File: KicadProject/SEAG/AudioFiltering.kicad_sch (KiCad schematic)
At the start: 8 parts, among them U2 ${SIM.PARAMS}

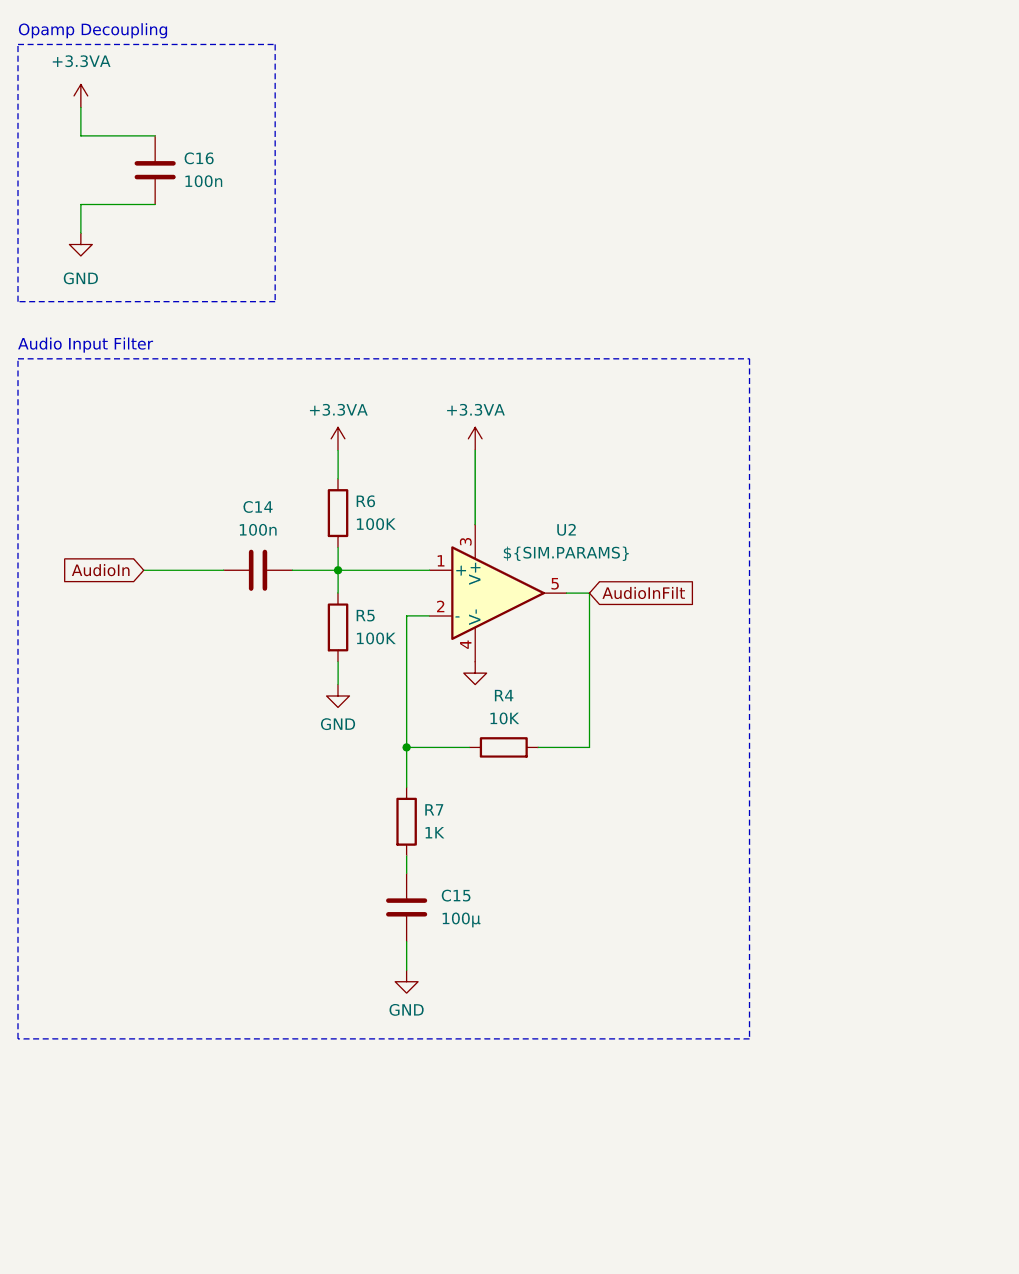
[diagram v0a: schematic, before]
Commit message: Added ESD protection, extra filtering with ferrite bead
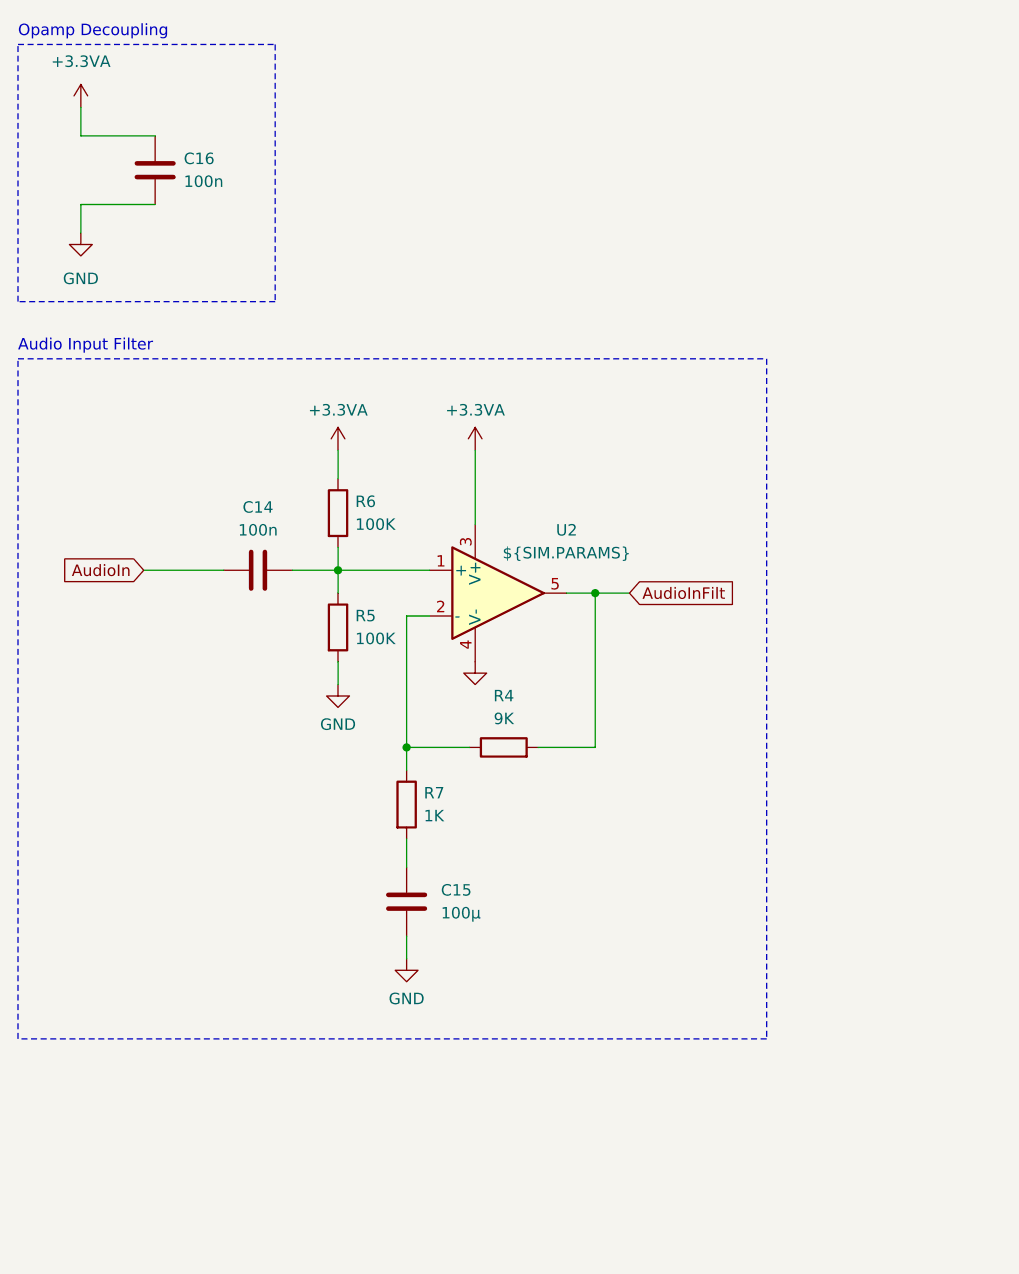
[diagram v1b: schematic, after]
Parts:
- R4: value 10K -> 9K
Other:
- moved on the sheet: C15, R7
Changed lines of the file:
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@@
 (kicad_sch (version 20230121) (generator eeschema)
   (paper "A4")
+  (junction (at 81.28 81.915) (diameter 0) (color 0 0 0 0)
+  )
   (junction (at 60.325 99.06) (diameter 0) (color 0 0 0 0)
   )
   (junction (at 52.705 79.375) (diameter 0) (color 0 0 0 0)
   )
-  (wire (pts (xy 74.93 99.06) (xy 80.645 99.06))
-    (stroke (width 0) (type default))
-  )
-  (wire (pts (xy 80.645 81.915) (xy 78.105 81.915))
+  (wire (pts (xy 74.93 99.06) (xy 81.28 99.06))
     (stroke (width 0) (type default))
   )
@@
     (stroke (width 0) (type default))
   )
-  (wire (pts (xy 60.325 99.06) (xy 60.325 103.505))
+  (wire (pts (xy 60.325 99.06) (xy 60.325 101.6))
+    (stroke (width 0) (type default))
+  )
+  (wire (pts (xy 81.28 81.915) (xy 85.09 81.915))
     (stroke (width 0) (type default))
   )
@@
     (stroke (width 0) (type default))
   )
-  (wire (pts (xy 60.325 111.125) (xy 60.325 113.03))
+  (wire (pts (xy 60.325 109.22) (xy 60.325 112.395))
     (stroke (width 0) (type default))
   )
@@
     (stroke (width 0) (type default))
   )
-  (wire (pts (xy 80.645 99.06) (xy 80.645 81.915))
-    (stroke (width 0) (type default))
-  )
-  (wire (pts (xy 60.325 120.65) (xy 60.325 123.825))
+  (wire (pts (xy 78.105 81.915) (xy 81.28 81.915))
+    (stroke (width 0) (type default))
+  )
+  (wire (pts (xy 60.325 120.015) (xy 60.325 122.555))
     (stroke (width 0) (type default))
   )
@@
     (stroke (width 0) (type default))
   )
-  (rectangle (start 17.145 55.88) (end 98.425 131.445)
+  (wire (pts (xy 81.28 81.915) (xy 81.28 99.06))
+    (stroke (width 0) (type default))
+  )
+  (rectangle (start 17.145 55.88) (end 100.33 131.445)
     (stroke (width 0) (type dash))
     (fill (type none))
@@
     )
   )
-  (global_label "AudioInFilt" (shape input) (at 80.645 81.915 0) (fields_autoplaced)
+  (global_label "AudioInFilt" (shape input) (at 85.09 81.915 0) (fields_autoplaced)
     (effects (font (size 1.27 1.27)) (justify left))
-    (property "Intersheetrefs" "${INTERSHEET_REFS}" (at 93.6087 81.915 0)
+    (property "Intersheetrefs" "${INTERSHEET_REFS}" (at 98.0537 81.915 0)
       (effects (font (size 1.27 1.27)) (justify left) hide)
     )
@@
     )
   )
-  (symbol (lib_id "Device:R") (at 60.325 107.315 0) (unit 1)
-    (in_bom yes) (on_board yes) (dnp no) (fields_autoplaced)
-    (property "Reference" "R7" (at 62.23 106.045 0)
-      (effects (font (size 1.27 1.27)) (justify left))
-    )
-    (property "Value" "1K" (at 62.23 108.585 0)
-      (effects (font (size 1.27 1.27)) (justify left))
-    )
-    (property "Footprint" "Resistor_SMD:R_0805_2012Metric" (at 58.547 107.315 90)
-      (effects (font (size 1.27 1.27)) hide)
-    )
-    (property "Datasheet" "~" (at 60.325 107.315 0)
+  (symbol (lib_id "Device:R") (at 60.325 105.41 0) (unit 1)
+    (in_bom yes) (on_board yes) (dnp no) (fields_autoplaced)
+    (property "Reference" "R7" (at 62.23 104.14 0)
+      (effects (font (size 1.27 1.27)) (justify left))
+    )
+    (property "Value" "1K" (at 62.23 106.68 0)
+      (effects (font (size 1.27 1.27)) (justify left))
+    )
+    (property "Footprint" "Resistor_SMD:R_0805_2012Metric" (at 58.547 105.41 90)
+      (effects (font (size 1.27 1.27)) hide)
+    )
+    (property "Datasheet" "~" (at 60.325 105.41 0)
       (effects (font (size 1.27 1.27)) hide)
     )
@@
     )
   )
-  (symbol (lib_id "power:GND") (at 60.325 123.825 0) (unit 1)
-    (in_bom yes) (on_board yes) (dnp no) (fields_autoplaced)
-    (property "Reference" "#PWR022" (at 60.325 130.175 0)
-      (effects (font (size 1.27 1.27)) hide)
-    )
-    (property "Value" "GND" (at 60.325 128.27 0)
-      (effects (font (size 1.27 1.27)))
-    )
-    (property "Footprint" "" (at 60.325 123.825 0)
-      (effects (font (size 1.27 1.27)) hide)
-    )
-    (property "Datasheet" "" (at 60.325 123.825 0)
+  (symbol (lib_id "power:GND") (at 60.325 122.555 0) (unit 1)
+    (in_bom yes) (on_board yes) (dnp no) (fields_autoplaced)
+    (property "Reference" "#PWR022" (at 60.325 128.905 0)
+      (effects (font (size 1.27 1.27)) hide)
+    )
+    (property "Value" "GND" (at 60.325 127 0)
+      (effects (font (size 1.27 1.27)))
+    )
+    (property "Footprint" "" (at 60.325 122.555 0)
+      (effects (font (size 1.27 1.27)) hide)
+    )
+    (property "Datasheet" "" (at 60.325 122.555 0)
       (effects (font (size 1.27 1.27)) hide)
     )
@@
       (effects (font (size 1.27 1.27)))
     )
-    (property "Value" "10K" (at 71.12 95.885 90)
+    (property "Value" "9K" (at 71.12 95.885 90)
       (effects (font (size 1.27 1.27)))
     )
@@
     )
   )
-  (symbol (lib_id "Device:C") (at 60.325 116.84 0) (unit 1)
-    (in_bom yes) (on_board yes) (dnp no) (fields_autoplaced)
-    (property "Reference" "C15" (at 64.135 115.57 0)
-      (effects (font (size 1.27 1.27)) (justify left))
-    )
-    (property "Value" "100µ" (at 64.135 118.11 0)
-      (effects (font (size 1.27 1.27)) (justify left))
-    )
-    (property "Footprint" "Capacitor_SMD:C_0805_2012Metric" (at 61.2902 120.65 0)
-      (effects (font (size 1.27 1.27)) hide)
-    )
-    (property "Datasheet" "~" (at 60.325 116.84 0)
-      (effects (font (size 1.27 1.27)) hide)
-    )
+  (symbol (lib_id "Device:C") (at 60.325 116.205 0) (unit 1)
+    (in_bom yes) (on_board yes) (dnp no) (fields_autoplaced)
+    (property "Reference" "C15" (at 64.135 114.935 0)
+      (effects (font (size 1.27 1.27)) (justify left))
+    )
+    (property "Value" "100µ" (at 64.135 117.475 0)
+      (effects (font (size 1.27 1.27)) (justify left))
+    )
+    (property "Footprint" "Capacitor_SMD:C_0805_2012Metric" (at 61.2902 120.015 0)
+      (effects (font (size 1.27 1.27)) hide)
+    )
+    (property "Datasheet" "~" (at 60.325 116.205 0)
+      (effects (font (size 1.27 1.27)) hide)
+    )

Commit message: Finished PCB, stil uncertain about couple things
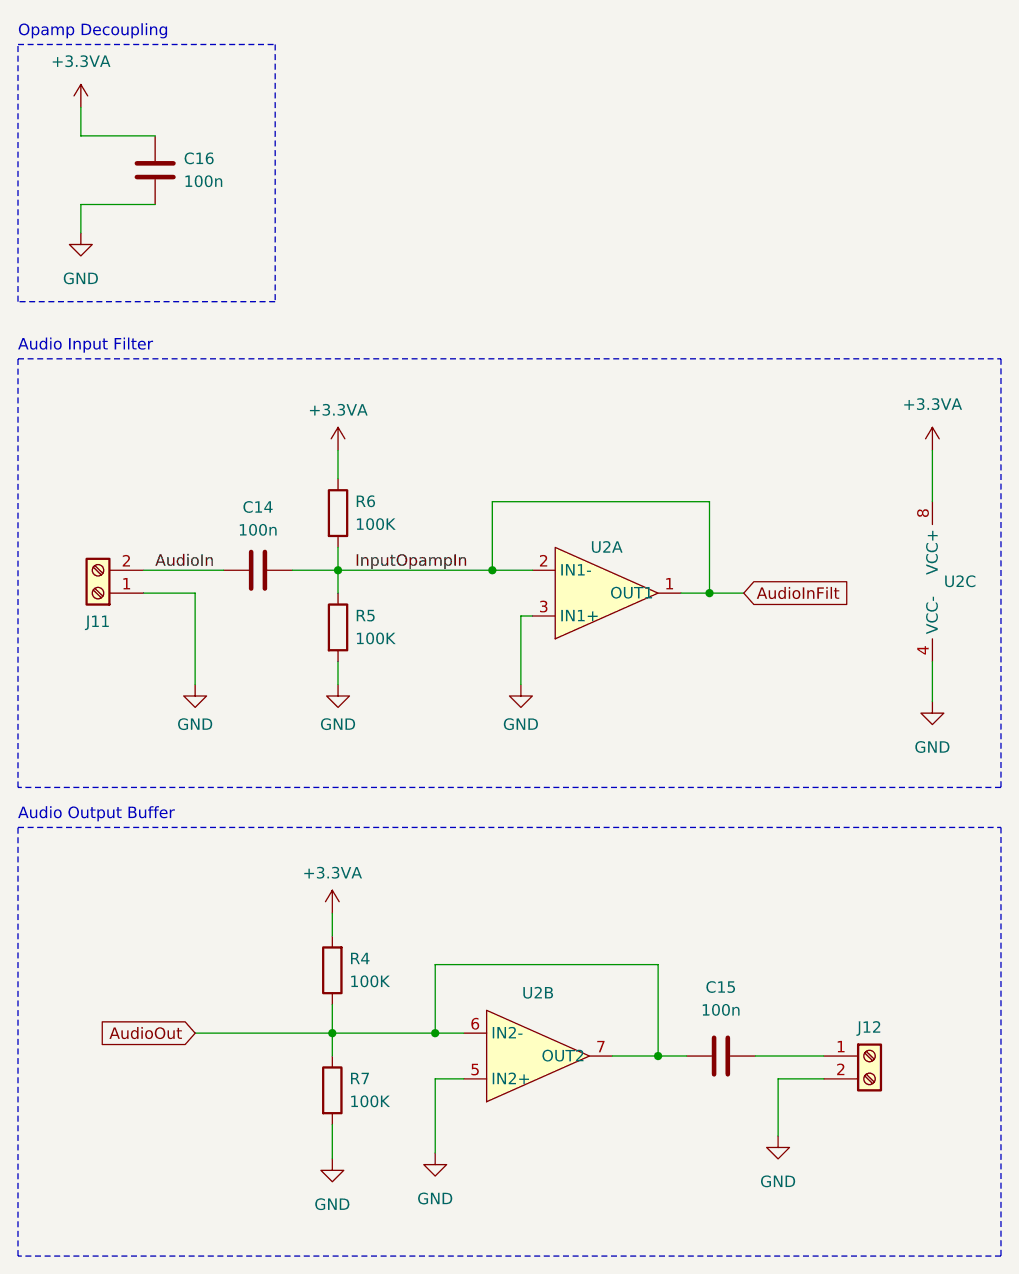
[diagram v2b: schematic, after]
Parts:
- removed U2: ${SIM.PARAMS}, symbol Simulation_SPICE:OPAMP
- added J11, J12: Screw_Terminal_01x02, TerminalBlock_Phoenix:TerminalBlock_Phoenix_MKDS-1,5-2_1x02_P5.00mm_Horizontal, symbol Connector:Screw_Terminal_01x02
- added U2: ~, SamacSys_Parts:SOIC127P600X175-8N, symbol MyLibrary:LM833DGKR_
- C15: value 100µ -> 100n
- R4: value 9K -> 100K
- R7: value 1K -> 100K
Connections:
- net +3.3VA: now also R4.2, U2.8 (VCC+)
- net AudioIn: now also J11.2 (Pin_2)
- net AudioInFilt: now also C14.2, R5.1, R6.2, U2.1 (OUT1), U2.2 (IN1-); no longer R4.2
- net GND: now also R7.2, J11.1 (Pin_1), J12.2 (Pin_2), U2.3 (IN1+), U2.4 (VCC-), U2.5 (IN2+); no longer C15.2
- net AudioOut: now reaches R4.1, R7.1
- net AudioOut: now also C15.1, U2.6 (IN2-), U2.7 (OUT2)
- new net: C15.2, J12.1 (Pin_1)
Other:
- note added: "Audio Output Buffer"

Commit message: PCB rev 2
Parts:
- renumbered C16 to C401, C14 to C402, C15 to C403, R6 to R401, R5 to R402, R4 to R403, R7 to R404
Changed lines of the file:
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@@
   (symbol (lib_id "Device:R") (at 52.07 123.825 180) (unit 1)
     (in_bom yes) (on_board yes) (dnp no) (fields_autoplaced)
-    (property "Reference" "R4" (at 53.975 122.555 0)
+    (property "Reference" "R403" (at 53.975 122.555 0)
       (effects (font (size 1.27 1.27)) (justify right))
     )
@@
       (project "SEAG"
         (path "/37e7da6e-dab5-4e62-b28a-754ec4806405/2395ecb5-6576-49c9-80ea-add07f3bcf94"
-          (reference "R4") (unit 1)
+          (reference "R403") (unit 1)
         )
       )
@@
   (symbol (lib_id "Device:R") (at 52.705 73.025 0) (unit 1)
     (in_bom yes) (on_board yes) (dnp no) (fields_autoplaced)
-    (property "Reference" "R6" (at 54.61 71.755 0)
+    (property "Reference" "R401" (at 54.61 71.755 0)
       (effects (font (size 1.27 1.27)) (justify left))
     )
@@
       (project "SEAG"
         (path "/37e7da6e-dab5-4e62-b28a-754ec4806405/2395ecb5-6576-49c9-80ea-add07f3bcf94"
-          (reference "R6") (unit 1)
+          (reference "R401") (unit 1)
         )
       )
@@
   (symbol (lib_id "Device:C") (at 43.815 79.375 90) (unit 1)
     (in_bom yes) (on_board yes) (dnp no) (fields_autoplaced)
-    (property "Reference" "C14" (at 43.815 72.39 90)
+    (property "Reference" "C402" (at 43.815 72.39 90)
       (effects (font (size 1.27 1.27)))
     )
@@
       (project "SEAG"
         (path "/37e7da6e-dab5-4e62-b28a-754ec4806405/2395ecb5-6576-49c9-80ea-add07f3bcf94"
-          (reference "C14") (unit 1)
+          (reference "C402") (unit 1)
         )
       )
@@
   (symbol (lib_id "Device:R") (at 52.07 137.16 0) (unit 1)
     (in_bom yes) (on_board yes) (dnp no) (fields_autoplaced)
-    (property "Reference" "R7" (at 53.975 135.89 0)
+    (property "Reference" "R404" (at 53.975 135.89 0)
       (effects (font (size 1.27 1.27)) (justify left))
     )
@@
       (project "SEAG"
         (path "/37e7da6e-dab5-4e62-b28a-754ec4806405/2395ecb5-6576-49c9-80ea-add07f3bcf94"
-          (reference "R7") (unit 1)
+          (reference "R404") (unit 1)
         )
       )
@@
   (symbol (lib_id "Device:C") (at 32.385 34.925 0) (unit 1)
     (in_bom yes) (on_board yes) (dnp no) (fields_autoplaced)
-    (property "Reference" "C16" (at 35.56 33.655 0)
+    (property "Reference" "C401" (at 35.56 33.655 0)
       (effects (font (size 1.27 1.27)) (justify left))
     )
@@
       (project "SEAG"
         (path "/37e7da6e-dab5-4e62-b28a-754ec4806405/2395ecb5-6576-49c9-80ea-add07f3bcf94"
-          (reference "C16") (unit 1)
+          (reference "C401") (unit 1)
         )
       )
@@
   (symbol (lib_id "Device:R") (at 52.705 85.725 0) (unit 1)
     (in_bom yes) (on_board yes) (dnp no) (fields_autoplaced)
-    (property "Reference" "R5" (at 54.61 84.455 0)
+    (property "Reference" "R402" (at 54.61 84.455 0)
       (effects (font (size 1.27 1.27)) (justify left))
     )
@@
       (project "SEAG"
         (path "/37e7da6e-dab5-4e62-b28a-754ec4806405/2395ecb5-6576-49c9-80ea-add07f3bcf94"
-          (reference "R5") (unit 1)
+          (reference "R402") (unit 1)
         )
       )
@@
   (symbol (lib_id "Device:C") (at 95.25 133.35 90) (unit 1)
     (in_bom yes) (on_board yes) (dnp no) (fields_autoplaced)
-    (property "Reference" "C15" (at 95.25 125.73 90)
+    (property "Reference" "C403" (at 95.25 125.73 90)
       (effects (font (size 1.27 1.27)))
     )
@@
       (project "SEAG"
         (path "/37e7da6e-dab5-4e62-b28a-754ec4806405/2395ecb5-6576-49c9-80ea-add07f3bcf94"
-          (reference "C15") (unit 1)
-        )
-      )
+          (reference "C403") (unit 1)
+        )
+      )

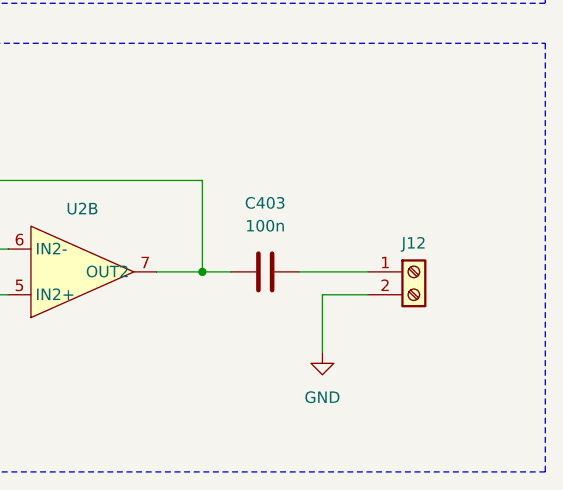
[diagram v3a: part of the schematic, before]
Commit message: Added rotary encoder screw terminal
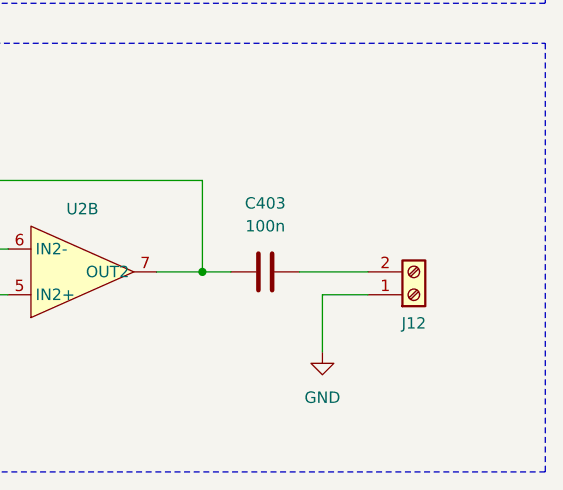
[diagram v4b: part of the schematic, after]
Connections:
- net GND: now also J12.1 (Pin_1); no longer J12.2 (Pin_2)
- net at C403.2: now also J12.2 (Pin_2); no longer J12.1 (Pin_1)
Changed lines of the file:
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@@
+    (stroke (width 0) (type default))
+  )
+  (wire (pts (xy 99.06 133.35) (xy 106.68 133.35))
     (stroke (width 0) (type default))
   )
@@
   )
   (wire (pts (xy 32.385 31.115) (xy 24.13 31.115))
-    (stroke (width 0) (type default))
-  )
-  (wire (pts (xy 99.06 133.35) (xy 106.68 133.35))
     (stroke (width 0) (type default))
   )
@@
     )
   )
-  (symbol (lib_id "Connector:Screw_Terminal_01x02") (at 111.76 133.35 0) (unit 1)
+  (symbol (lib_id "Connector:Screw_Terminal_01x02") (at 111.76 135.89 0) (mirror x) (unit 1)
     (in_bom yes) (on_board yes) (dnp no)
-    (property "Reference" "J12" (at 111.76 130.175 0)
-      (effects (font (size 1.27 1.27)))
-    )
-    (property "Value" "Screw_Terminal_01x02" (at 106.68 125.73 0)
-      (effects (font (size 1.27 1.27)) hide)
-    )
-    (property "Footprint" "TerminalBlock_Phoenix:TerminalBlock_Phoenix_MKDS-1,5-2_1x02_P5.00mm_Horizontal" (at 111.76 133.35 0)
-      (effects (font (size 1.27 1.27)) hide)
-    )
-    (property "Datasheet" "~" (at 111.76 133.35 0)
-      (effects (font (size 1.27 1.27)) hide)
-    )
+    (property "Reference" "J12" (at 111.76 139.065 0)
+      (effects (font (size 1.27 1.27)))
+    )
+    (property "Value" "Screw_Terminal_01x02" (at 106.68 143.51 0)
+      (effects (font (size 1.27 1.27)) hide)
+    )
+    (property "Footprint" "TerminalBlock_Phoenix:TerminalBlock_Phoenix_MKDS-1,5-2_1x02_P5.00mm_Horizontal" (at 111.76 135.89 0)
+      (effects (font (size 1.27 1.27)) hide)
+    )
+    (property "Datasheet" "~" (at 111.76 135.89 0)
+      (effects (font (size 1.27 1.27)) hide)
+    )

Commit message: Added header
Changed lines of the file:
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@@
-    (effects (font (size 1.27 1.27)) (justify left bottom))
-  )
-  (label "InputOpampIn" (at 54.61 79.375 0) (fields_autoplaced)
     (effects (font (size 1.27 1.27)) (justify left bottom))
   )
@@
     )
   )
-  (symbol (lib_id "MyLibrary:LM833DGKR_") (at 74.295 133.35 0) (unit 2)
+  (symbol (lib_name "LM833DGKR__2") (lib_id "MyLibrary:LM833DGKR_") (at 74.295 133.35 0) (unit 2)
     (in_bom yes) (on_board yes) (dnp no) (fields_autoplaced)
     (property "Reference" "U2" (at 74.93 126.365 0)
